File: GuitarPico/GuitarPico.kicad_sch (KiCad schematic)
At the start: 125 parts, among them J1 INPUT, J2 INPUT, J3 OUTPUT, J4 OUTPUT, J5 Barrel_Jack_Switch, J6 VGA, J8 INPUT, J9 INPUT, Q1 2N3904, Q2 2N3904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

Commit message: Working pass thru
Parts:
- added C32, C33: 220 uF, Capacitor_THT:CP_Radial_D5.0mm_P2.50mm, symbol Device:C_Polarized_Small
- added R58: 10R, Resistor_THT:R_Axial_DIN0207_L6.3mm_D2.5mm_P7.62mm_Horizontal, symbol Device:R
- C9: value 47 pF -> 220 pF
- R24: value 10k -> 100
- R9: value 10k -> 47k
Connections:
- net +3V3: now also R58.1; no longer Brd1.2 (VCC), C24.2
- net GND: now also C32.2, C33.2
- net at C17.1, R19.1, R20.2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: now also RV2.3; no longer RV2.1
- net at C7.2, R7.1, R8.2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: now also RV1.3; no longer RV1.1
- net at R5.1, R7.2, RV1.2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: now also RV1.1; no longer RV1.3
- net at R17.1, R19.2, RV2.2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: now also RV2.1; no longer RV2.3
- new net: Brd1.2 (VCC), C24.2, C32.1, C33.1, R58.2
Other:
- moved on the sheet: Brd1, C24, R36, R37, RV1, RV2

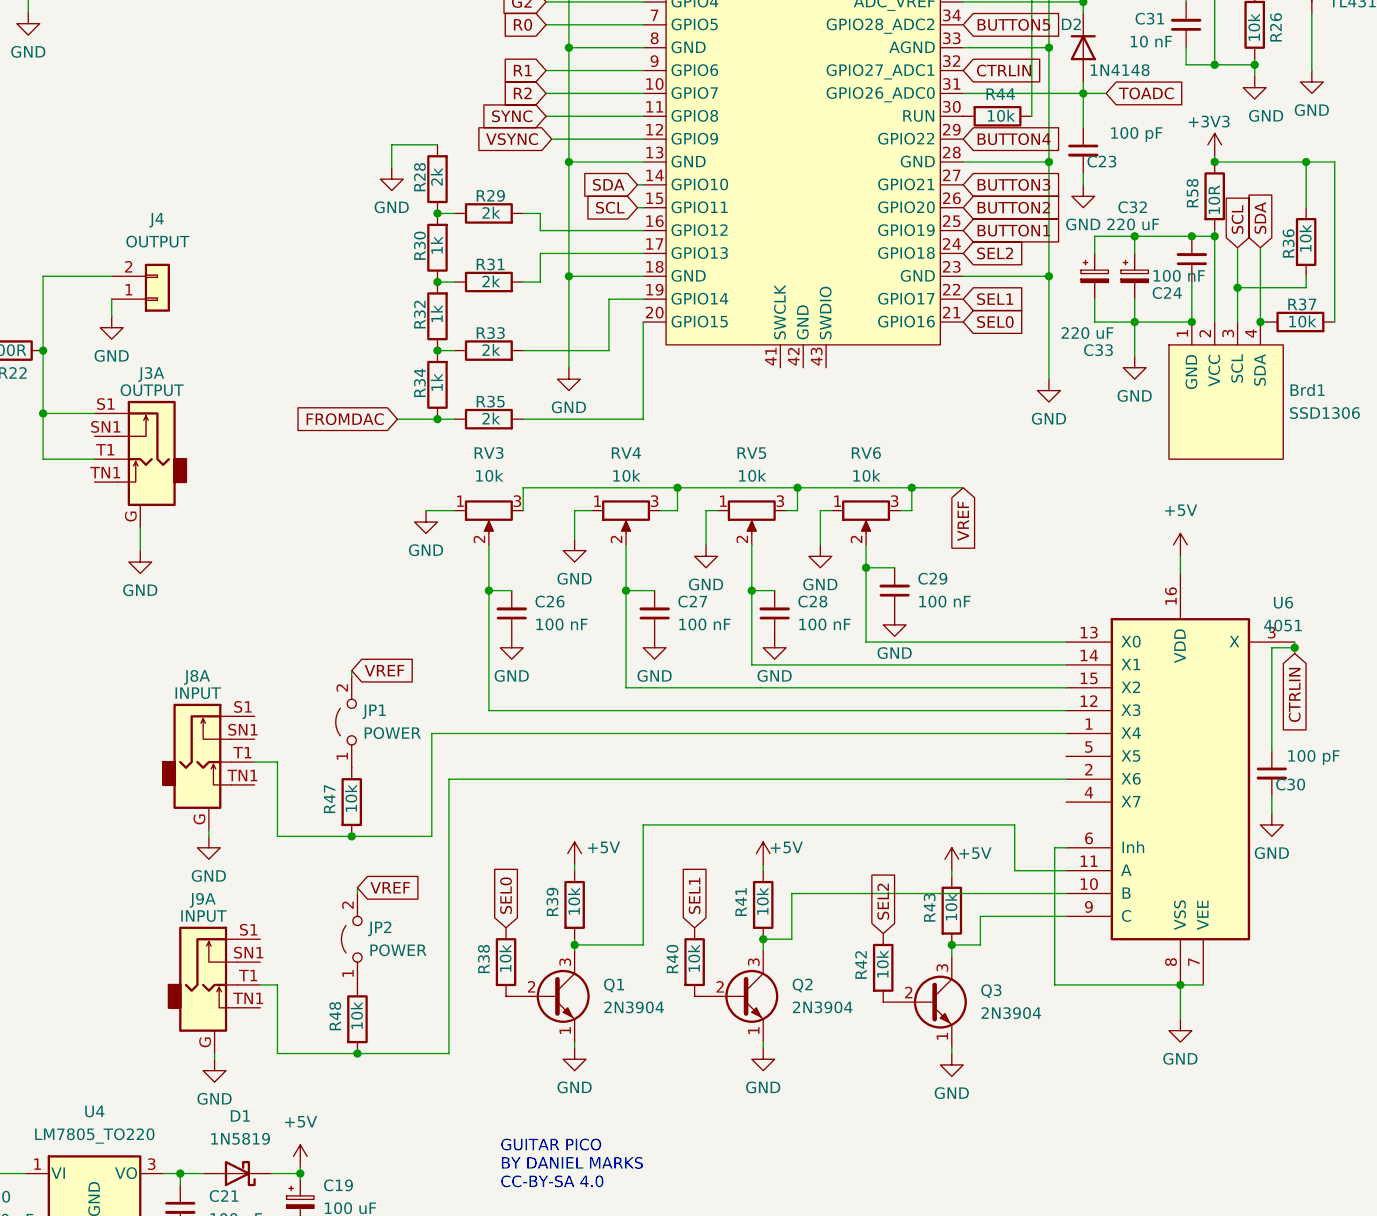
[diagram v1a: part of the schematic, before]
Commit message: Added ui elements
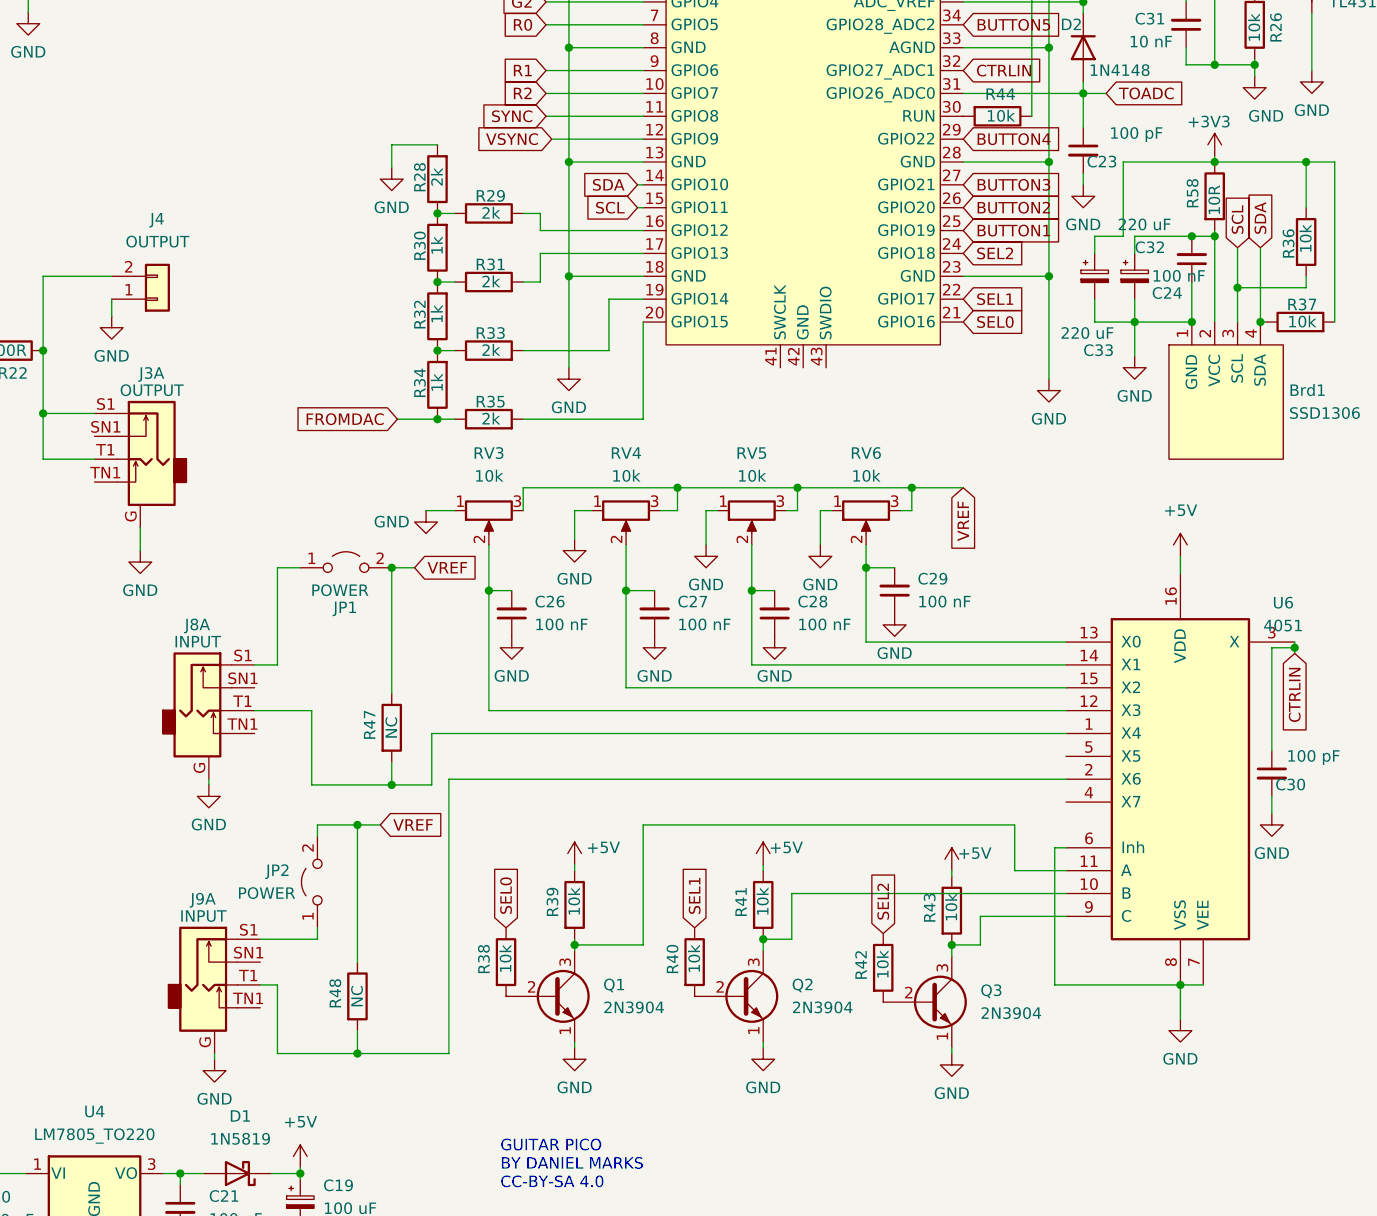
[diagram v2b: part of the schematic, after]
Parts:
- R47, R48: value 10k -> NC
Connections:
- net +3V3: now also C33.1
- net VREF: now also R47.1, R48.1
- net at Brd1.2 (VCC), C24.2, C32.1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: no longer C33.1
- net at JP1.1 (A): now also J8.S1; no longer R47.1
- net at JP2.1 (A): now also J9.S1; no longer R48.1
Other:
- moved on the sheet: J8A, JP1, JP2, R47, R48

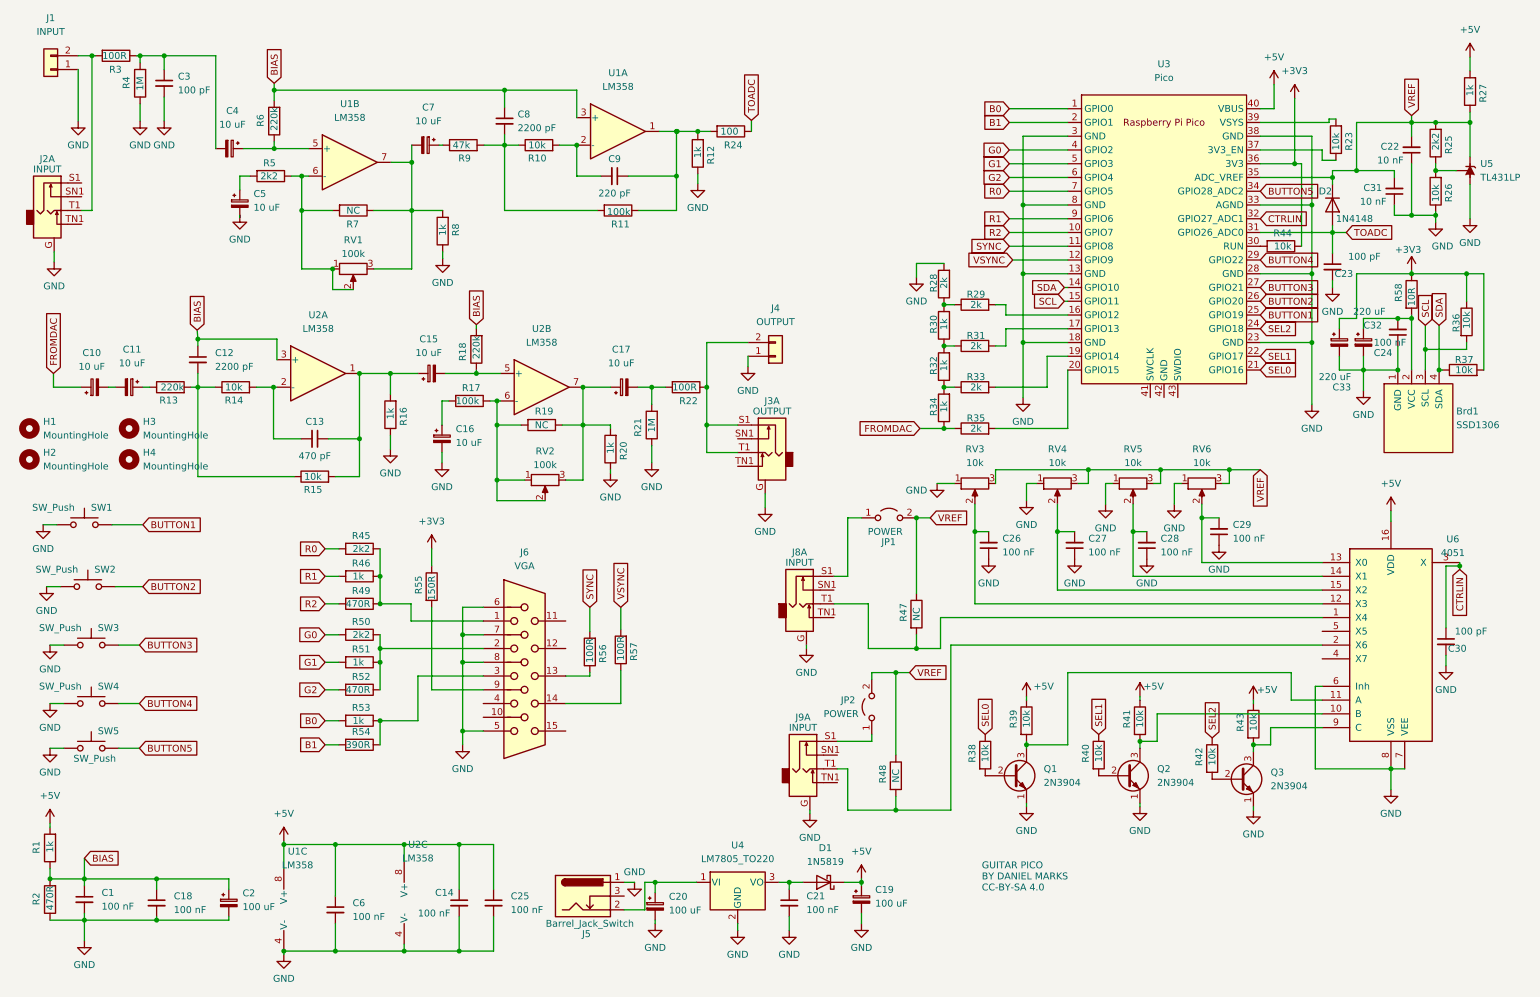
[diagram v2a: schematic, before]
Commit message: can now edit parameters
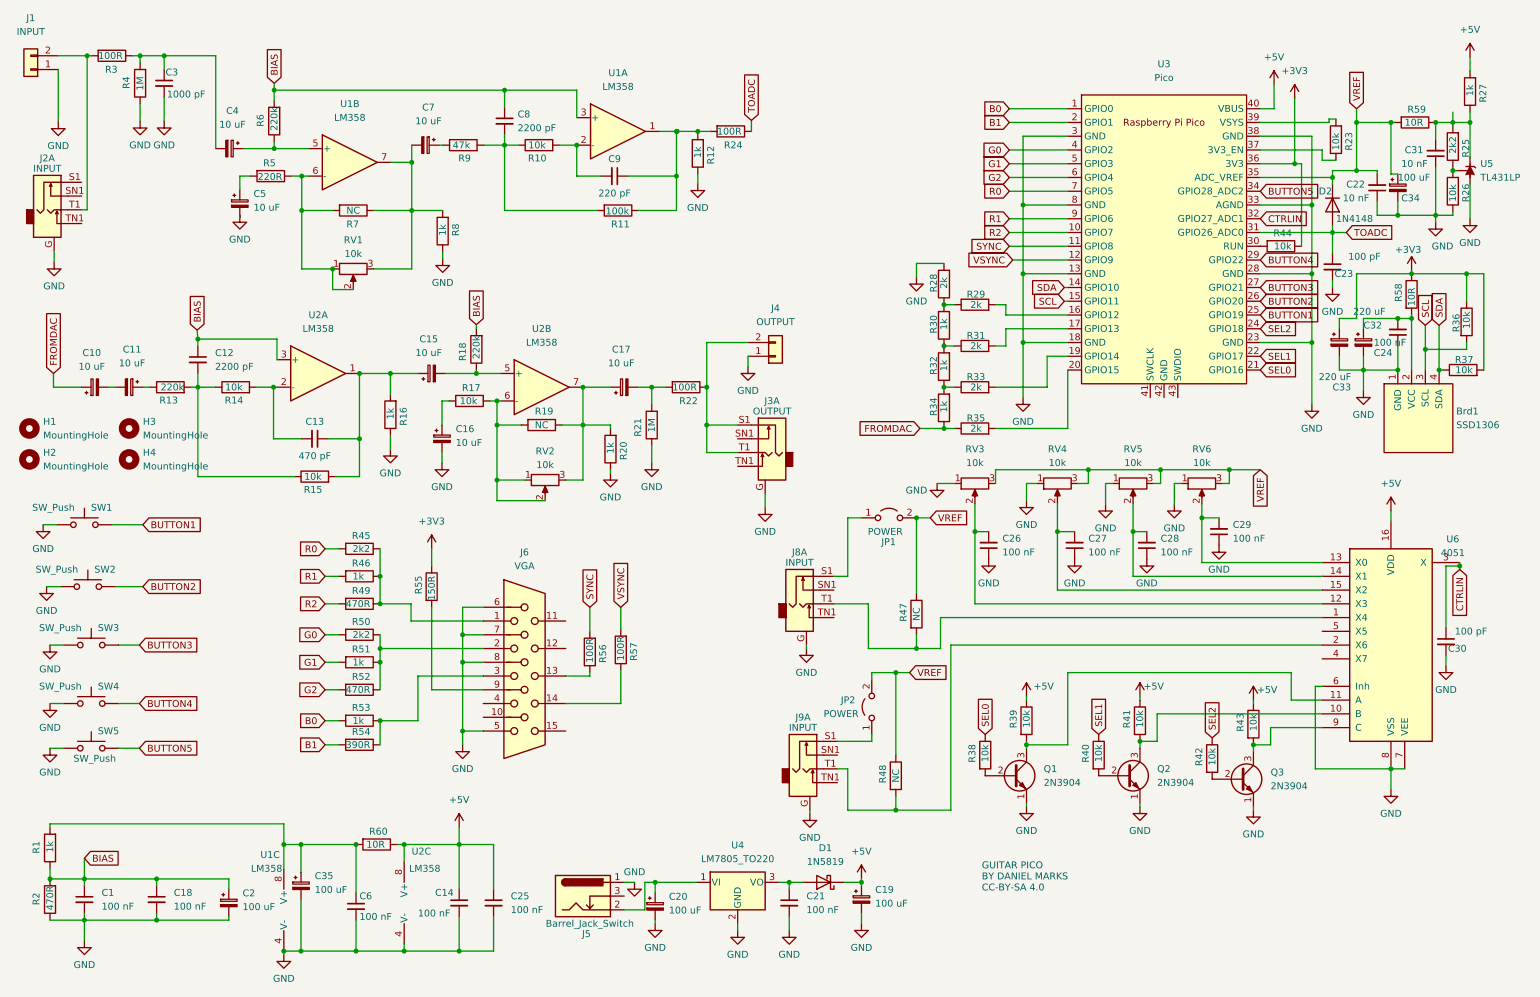
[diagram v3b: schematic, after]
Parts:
- added C34, C35: 100 uF, Capacitor_THT:CP_Radial_D5.0mm_P2.50mm, symbol Device:C_Polarized_Small
- added R59, R60: 10R, Resistor_THT:R_Axial_DIN0207_L6.3mm_D2.5mm_P7.62mm_Horizontal, symbol Device:R
- C3: value 100 pF -> 1000 pF
- R17, RV1, RV2: value 100k -> 10k
- R24: value 100 -> 100R
- R5: value 2k2 -> 220R
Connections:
- net +5V: now also R60.1; no longer C6.1, R1.2, U1.8 (V+)
- net GND: now also C34.2, C35.2; no longer J2.G
- net VREF: now also C34.1, R59.2; no longer C31.2, R25.2, R27.1, U5.3 (K)
- new net: C31.2, R25.2, R27.1, R59.1, U5.3 (K)
- new net: C35.1, C6.1, R1.2, R60.2, U1.8 (V+)
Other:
- moved on the sheet: C18, C22, C31, C6, J1, R25, R26, R3

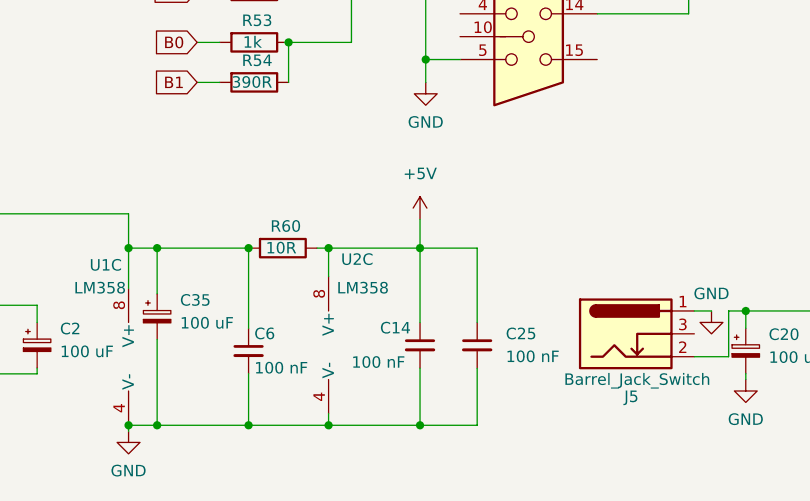
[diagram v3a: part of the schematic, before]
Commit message: Added room guitar effect
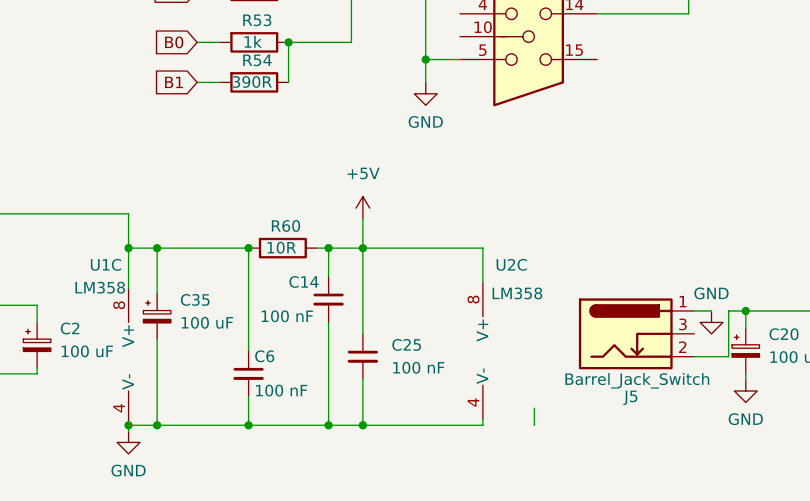
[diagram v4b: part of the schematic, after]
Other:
- moved on the sheet: C14, C25, C6, U2C

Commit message: Minor code fixes
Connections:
- net GND: now also J2.G
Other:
- moved on the sheet: C7, R9
